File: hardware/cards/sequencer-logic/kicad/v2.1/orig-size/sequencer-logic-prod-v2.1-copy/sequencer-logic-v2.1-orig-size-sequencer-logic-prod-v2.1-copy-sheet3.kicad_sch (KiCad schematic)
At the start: 8 parts, among them IC11 74*04, IC12 74*08, IC21 74*02, IC22 74*74, IC24 74*32

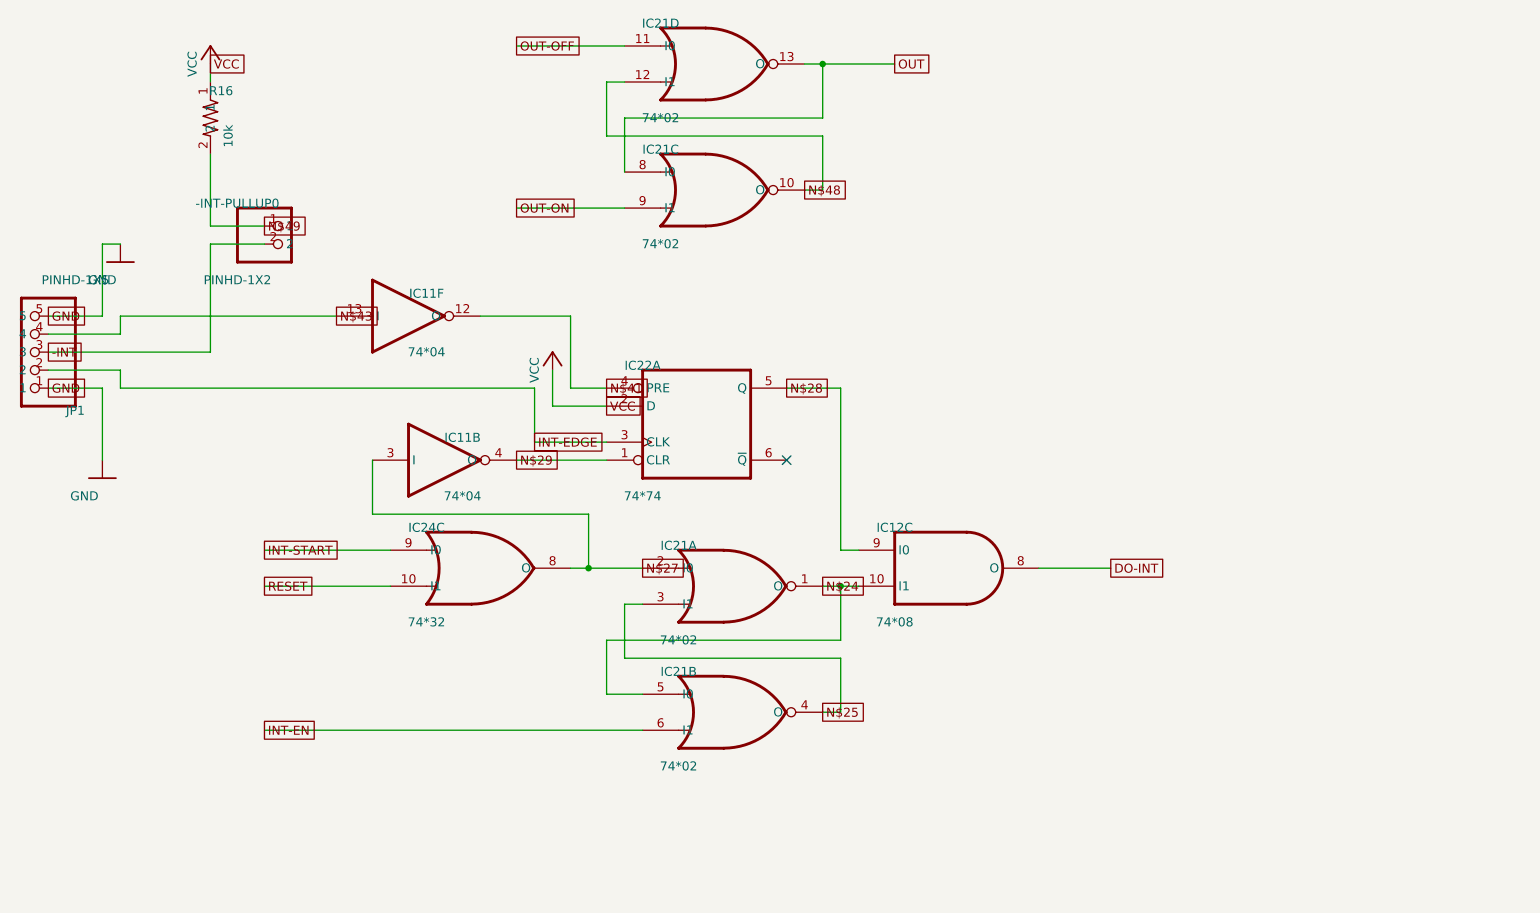
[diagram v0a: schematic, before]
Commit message: fix(kicad): readable converted schematics - overlaps 42,847 -> 3,147, nothing off the frame; CF sheet 0 overlaps
- tools/kicad/sch_overlaps.py: calibrated readability check (text/text, text/body, text/line, off frame/title block)
- eagle_sch_to_kicad.py: fields placed from Eagle's smashed attributes or the symbol's >NAME/>VALUE with Eagle's align,
  size and ratio, readable angles; fields Eagle never shows hidden (FABC96R shows only its pin name); pin numbers hidden
  where every Eagle pin hides them; Eagle-hidden layers dropped (the stray SpiceOrder text); labels on their own wires,
  converter labels only where KiCad needs them; rotate-then-mirror fixed for MR90/MR270 in pin_world/no-connects;
  each sheet on the smallest page that holds it, centred clear of the title block
- finish_board.py: stable footprint-library choice (DRC counts no longer vary run to run)
- all 37 projects regenerated: netlist proofs unchanged (34 MATCH, 2 schematic-only, video Fusion export MISMATCH as
  before); DRC same or better; ERC up (loose wire ends onto graphic buses no longer hidden by labels; explained per README)
- CF card: gate names off the gate bodies, U3 clear of its title, 5.08 mm connector pins; rebuilt: DRC 0/0, proof MATCH
- schematic PDFs regenerated (tools/sch_to_pdf.py, 37/37)

Co-Authored-By: Claude Opus 5.5 <noreply@anthropic.com>
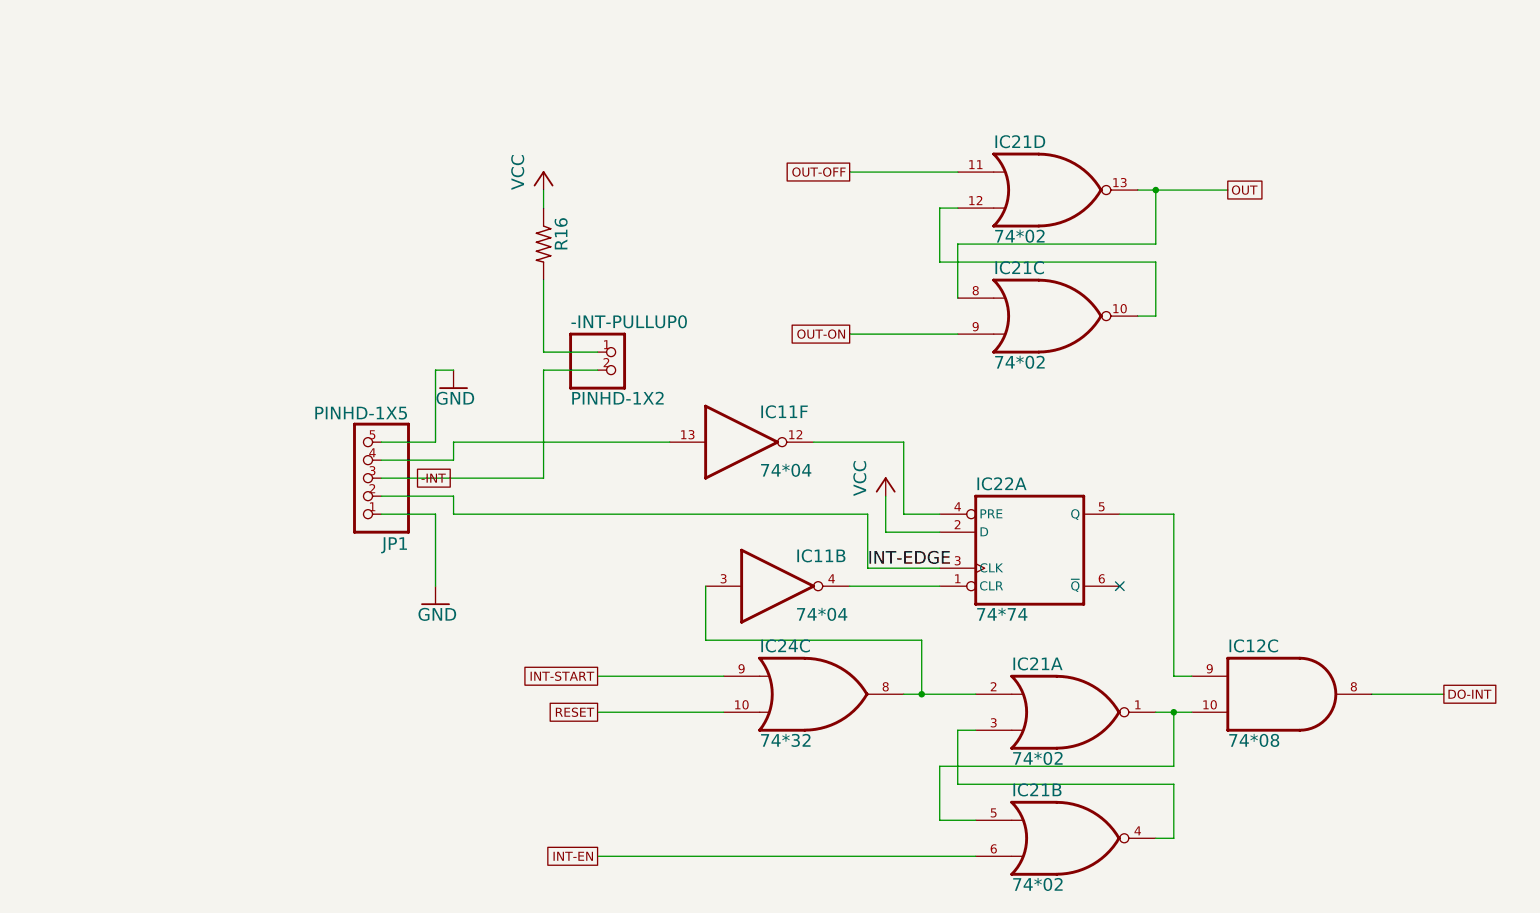
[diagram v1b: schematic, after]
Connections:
- net N$24: no longer names the net of IC12.10 (I1), IC21.1 (O), IC21.5 (I0)
- net N$25: no longer names the net of IC21.3 (I1), IC21.4 (O)
- net N$27: no longer names the net of IC11.3 (I), IC21.2 (I0), IC24.8 (O)
- net N$28: no longer names the net of IC12.9 (I0), IC22.5 (Q)
- net N$29: no longer names the net of IC11.4 (O), IC22.1 (CLR)
- net N$41: no longer names the net of IC11.12 (O), IC22.4 (PRE)
- net N$43: no longer names the net of IC11.13 (I), JP1.4
- net N$48: no longer names the net of IC21.10 (O), IC21.12 (I1)
- net N$49: no longer names the net of -INT-PULLUP0.1, R16.2
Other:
- moved on the sheet: IC22A
